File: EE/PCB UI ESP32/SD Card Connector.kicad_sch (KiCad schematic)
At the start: 3 parts, among them U11 693063020911

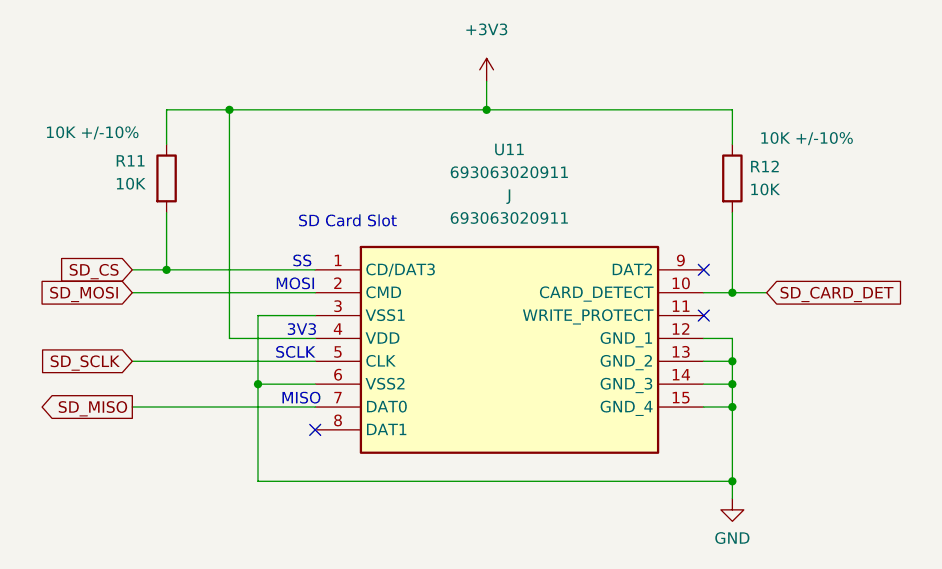
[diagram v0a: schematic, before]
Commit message: Finished first draft of ESP32-UI board
And moved around footprints, 3D models, etc. to match.
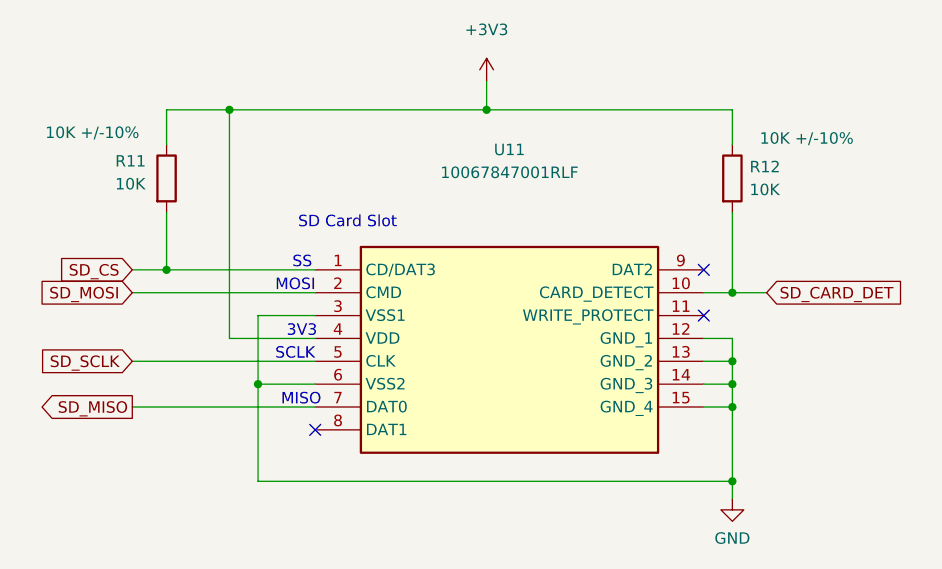
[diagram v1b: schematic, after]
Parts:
- U11: value 693063020911 -> 10067847001RLF; footprint 6930630220911:693063020911 -> DaisyBio_Mira:10067847001RLF; Datasheet_1 http://katalog.we-online.com/em/datasheet/693063020911.pdf -> (none); Footprint_1 693063020911 -> (none); Manufacturer_Name Wurth Elektronik -> (none); Manufacturer_Part_Number 693063020911 -> (none); Mouser Part Number 710-693063020911 -> (none); Mouser Price/Stock https://www.mouser.co.uk/ProductDetail/Wurth-Elektronik/693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 -> (none); Reference_1 J -> (none); Value_1 693063020911 -> (none)
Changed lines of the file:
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@@
 			)
 		)
-		(property "Value" "693063020911"
+		(property "Value" "10067847001RLF"
 			(at 142.24 67.31 0)
 			(effects
@@
 			)
 		)
-		(property "Footprint" "6930630220911:693063020911"
+		(property "Footprint" "DaisyBio_Mira:10067847001RLF"
 			(at 120.65 78.105 0)
 			(effects
@@
 			)
 		)
-		(property "Datasheet" "https://4donline.ihs.com/images/VipMasterIC/IC/MIDC/MIDC-S-A0011718380/MIDC-S-A0011718929-1.pdf?hkey=EF798316E3902B6ED9A73243A3159BB0"
+		(property "Datasheet" ""
 			(at 120.65 78.105 0)
 			(effects
@@
 				(hide yes)
 			)
-		)
-		(property "Reference_1" "J"
-			(at 142.24 69.85 0)
-			(effects
-				(font
-					(size 1.27 1.27)
-				)
-			)
-		)
-		(property "Value_1" "693063020911"
-			(at 142.24 72.39 0)
-			(effects
-				(font
-					(size 1.27 1.27)
-				)
-			)
-		)
-		(property "Footprint_1" "693063020911"
-			(at 160.02 173.025 0)
-			(effects
-				(font
-					(size 1.27 1.27)
-				)
-				(justify left top)
-				(hide yes)
-			)
-		)
-		(property "Datasheet_1" "http://katalog.we-online.com/em/datasheet/693063020911.pdf"
-			(at 160.02 273.025 0)
-			(effects
-				(font
-					(size 1.27 1.27)
-				)
-				(justify left top)
-				(hide yes)
-			)
-		)
-		(property "Height" ""
-			(at 160.02 473.025 0)
-			(effects
-				(font
-					(size 1.27 1.27)
-				)
-				(justify left top)
-				(hide yes)
-			)
-		)
-		(property "Manufacturer_Name" "Wurth Elektronik"
-			(at 160.02 573.025 0)
-			(effects
-				(font
-					(size 1.27 1.27)
-				)
-				(justify left top)
-				(hide yes)
-			)
-		)
-		(property "Manufacturer_Part_Number" "693063020911"
-			(at 160.02 673.025 0)
-			(effects
-				(font
-					(size 1.27 1.27)
-				)
-				(justify left top)
-				(hide yes)
-			)
-		)
-		(property "Mouser Part Number" "710-693063020911"
-			(at 160.02 773.025 0)
-			(effects
-				(font
-					(size 1.27 1.27)
-				)
-				(justify left top)
-				(hide yes)
-			)
-		)
-		(property "Mouser Price/Stock" "https://www.mouser.co.uk/ProductDetail/Wurth-Elektronik/693063020911?qs=7gQLVZk5cPm1OS%252BvOh%252BXTA%3D%3D"
-			(at 160.02 873.025 0)
-			(effects
-				(font
-					(size 1.27 1.27)
-				)
-				(justify left top)
-				(hide yes)
-			)
-		)
-		(property "Arrow Part Number" ""
-			(at 160.02 973.025 0)
-			(effects
-				(font
-					(size 1.27 1.27)
-				)
-				(justify left top)
-				(hide yes)
-			)
-		)
-		(property "Arrow Price/Stock" ""
-			(at 160.02 1073.025 0)
-			(effects
-				(font
-					(size 1.27 1.27)
-				)
-				(justify left top)
-				(hide yes)
-			)

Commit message: Finished V1 of ESP-UI
This is the version of ESP-UI that was ordered July 20 2025.
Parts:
- removed U11: 10067847001RLF, DaisyBio_Mira:10067847001RLF, symbol 693063020911:693063020911
- added J5: 10067847-001RLF, DaisyBio_Mira:10067847001RLF, symbol DaisyBio_Mira:10067847-001RLF
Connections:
- net +3V3: now also J5.4 (VDD)
- net GND: now also J5.3 (VSS_1), J5.6 (VSS_2), J5.GND
- net SD_CARD_DET: now also J5.CD (CD1)
- net SD_CS: now also J5.1 (CD/DAT3)
- net SD_MISO: now also J5.7 (DAT0)
- net SD_MOSI: now also J5.2 (CMD)
- net SD_SCLK: now also J5.5 (CLK)
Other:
- moved on the sheet: R11, R12
